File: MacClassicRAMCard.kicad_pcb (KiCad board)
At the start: 2 copper layers, 58.4 x 46 mm, 23 parts, among them J1 RAM Exp., U1 AS4C1M16F5, U2 AS4C1M16F5, U3 74HCT08D

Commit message: No actually
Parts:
- removed the FID1 at (93.0, 118.4)
- removed FID6: Fiducial, stdpads:Fiducial
- removed the H2 at (93.0, 115.8)
- removed the H3 at (148.3, 115.8)
- moved FID2 12.5 mm to (147.1, 130.8)
- moved FID3 5.08 mm to (150.9, 90.4)
- moved FID4 5.08 mm to (90.4, 90.4)
- moved H4 5.08 mm to (87.9, 90.4)
- moved H3 5.08 mm to (153.4, 90.4)
- moved FID1 3.59 mm to (94.2, 130.8)
- renumbered FID5 to FID1, FID4 to FID3, FID3 to FID4, H5 to H1, H6 to H2, H4 to H3, H1 to H4
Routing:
- net GND: vias 162 -> 176
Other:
- board size 58.4 x 46 mm -> 68.6 x 46 mm

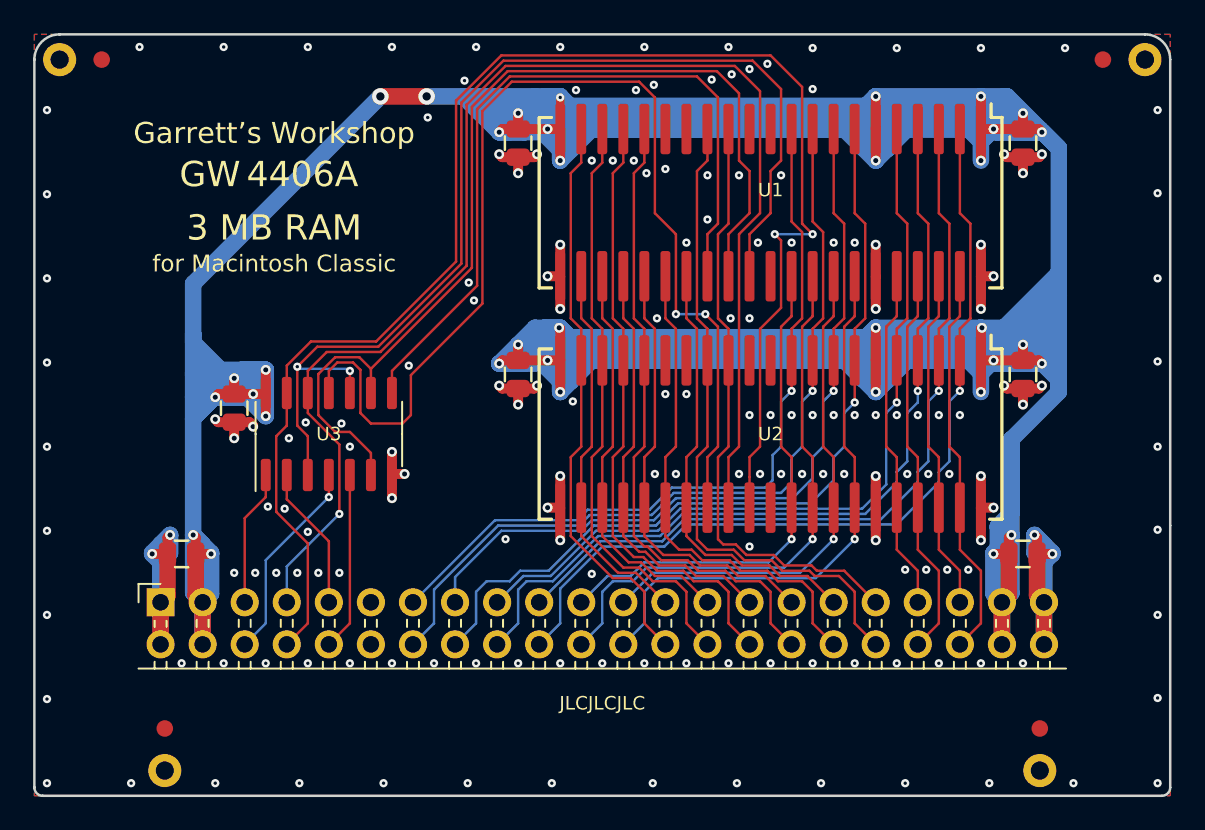
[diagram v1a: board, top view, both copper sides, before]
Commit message: Migrate to KiCAD 6
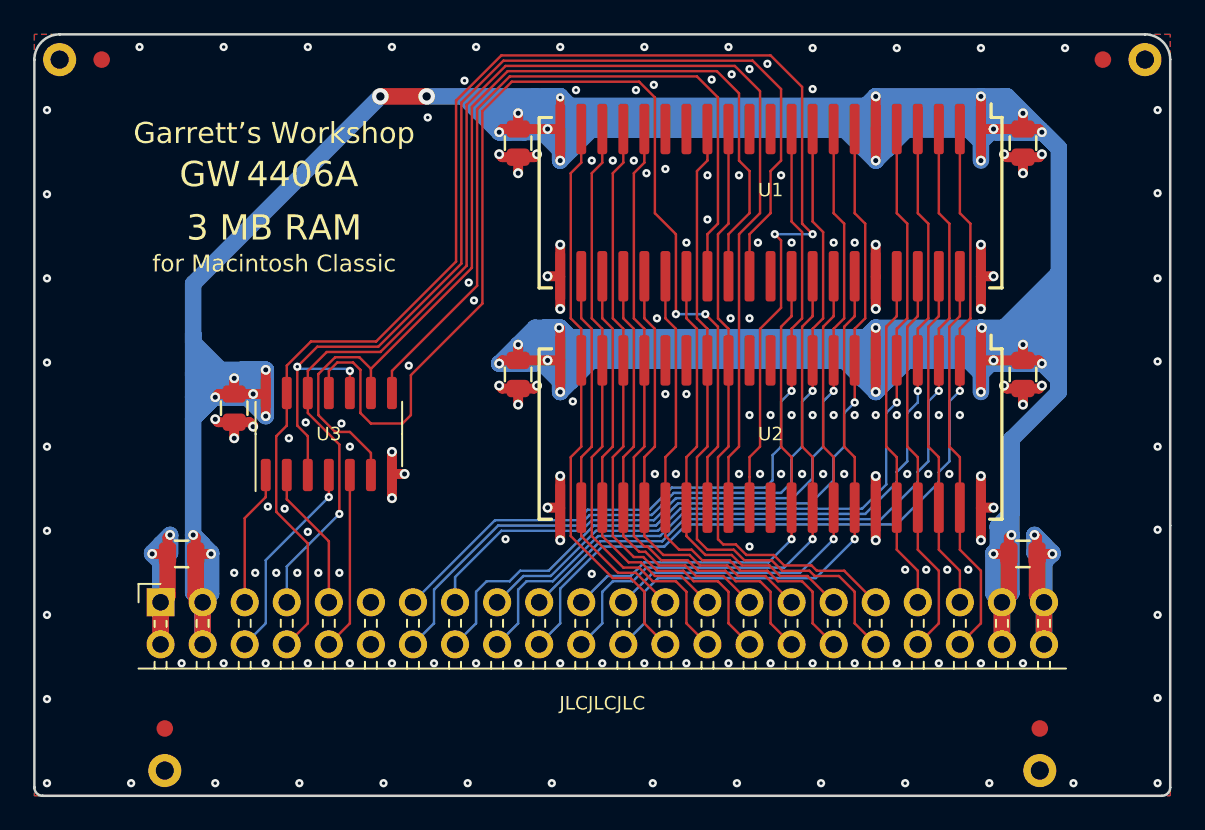
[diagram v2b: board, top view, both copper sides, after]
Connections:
- net /L~CAS~0 renamed /L~{CAS}0
- net /L~CAS~1 renamed /L~{CAS}1
- net /L~CAS~C renamed /L~{CAS}C
- net /L~CAS~D renamed /L~{CAS}D
- net /U~CAS~0 renamed /U~{CAS}0
- net /U~CAS~1 renamed /U~{CAS}1
- net /U~CAS~C renamed /U~{CAS}C
- net /U~CAS~D renamed /U~{CAS}D
- net /~OE~0 renamed /~{OE}0
- net /~OE~1 renamed /~{OE}1
- net /~RAS~ renamed /~{RAS}
- net /~WE~ renamed /~{WE}
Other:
- net class Default removed
